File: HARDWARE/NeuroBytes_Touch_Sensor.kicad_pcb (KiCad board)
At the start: 2 copper layers, 52.3 x 34.9 mm, 25 parts, among them P12 CONN_01X07, P6 CONN_01X04, P7 CONN_01X04, Q1 NPN_dual, Q2 NPN_dual, SW1 SW_PUSH, SW2 SW_PUSH, U1 STM32L011Gx, U2 LD3985G33R

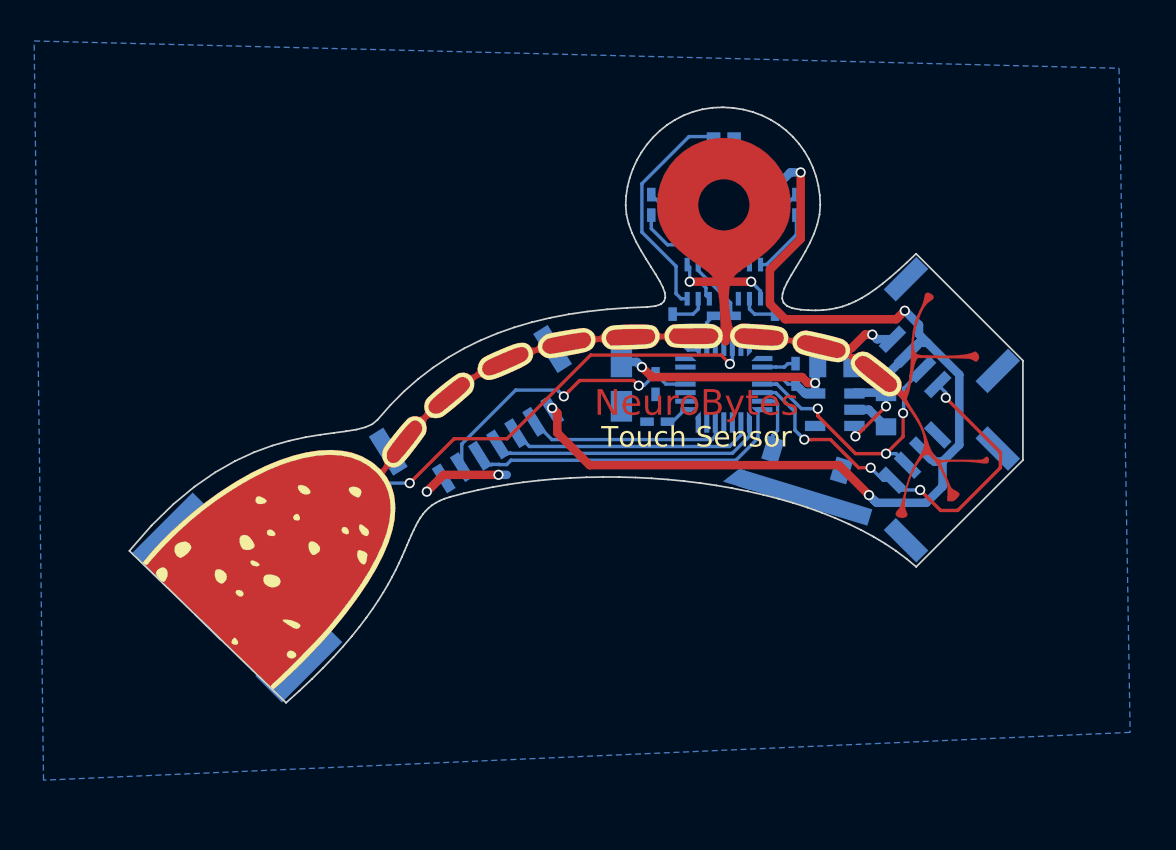
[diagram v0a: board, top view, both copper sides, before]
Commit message: Board rev2. Simplified PCB outline and modified axon graphics a bit.
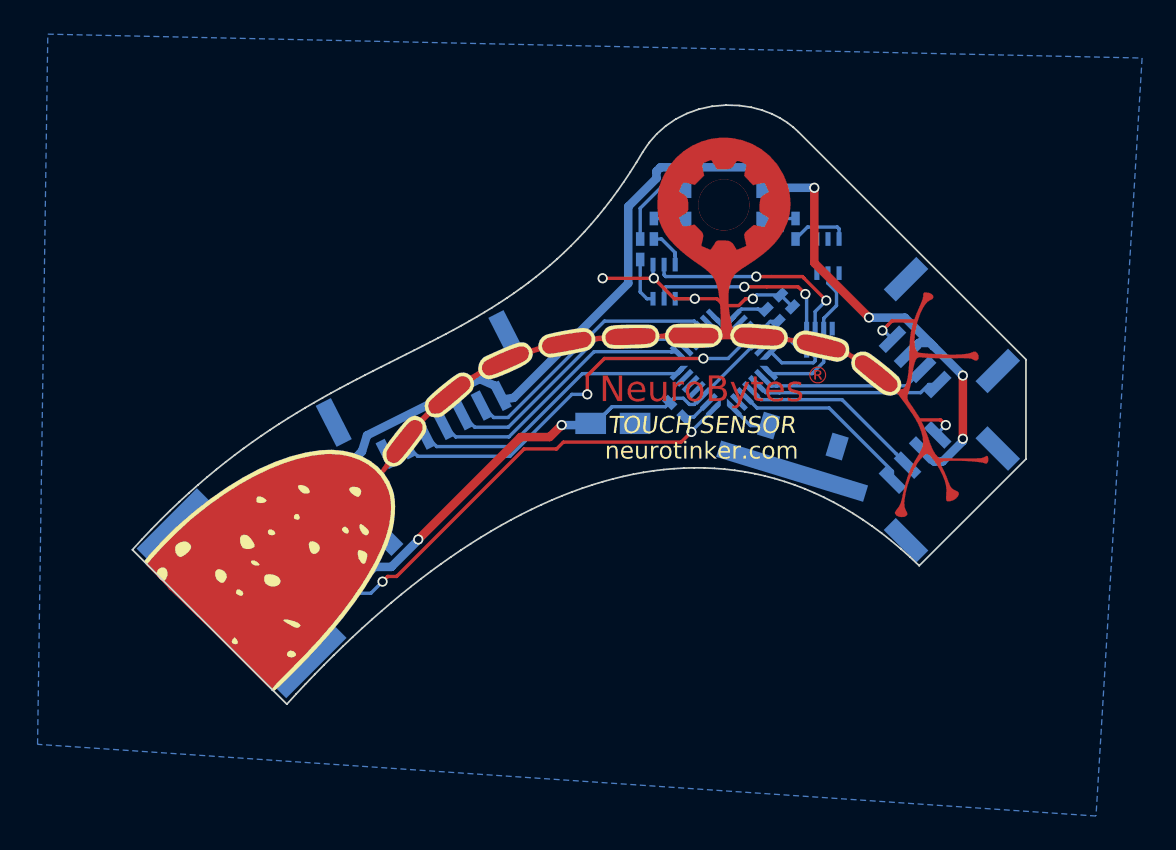
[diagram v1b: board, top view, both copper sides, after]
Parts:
- removed the G*** at (126.5, 69.5) (x3)
- removed R5, R6, R7: R, KiCad_Footprints:ZF_SMD_NonPol_0402
- added G***: LOGO, KiCad_Footprints:ZF_LOGO_Touch_Sensor, F.Cu at (126.5, 69.5)
- added RN1: R_Pack04, KiCad_Footprints:ZF_RN_4iso_CTS-0804, B.Cu at (132.1, 77.4)
- moved C1 33.6 mm to (102.8, 86.5), turned to 225 degrees
- moved U2 29.3 mm to (104.5, 88.2), turned to 315 degrees
- moved C4 28.9 mm to (106.2, 90.0), turned to 45 degrees
- moved R4 9.76 mm to (129.4, 75.2), turned to 225 degrees
- moved C5 8.64 mm to (130.1, 75.9), turned to 45 degrees
- moved R1 8.22 mm to (121.6, 72.1), turned to 270 degrees
- moved C3 7.26 mm to (123.8, 81.5), turned to 315 degrees
- moved Q2 4.84 mm to (132.6, 72.5)
- moved P12 3.25 mm to (109.0, 80.2), turned to 117 degrees
- moved C2 2.35 mm to (120.0, 82.3), turned to 0 degrees
- moved Q1 2.00 mm to (123.0, 74.0)
- moved SW1 1.42 mm to (130.4, 85.6)
- moved R2 1.41 mm to (122.4, 70.9)
- moved R3 1.40 mm to (130.7, 70.9)
- moved U1 1.25 mm to (126.5, 78.8), turned to 225 degrees
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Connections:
- P6 pad 3: AIN -> A1IN
- P6 pad 4: AEX -> A1EX
- P7 pad 3: AIN -> A2IN
- P7 pad 4: AEX -> A2EX
- U1 pad 10: Net-(U1-Pad10) -> A1EX
- U1 pad 11: LED_G -> A2IN
- U1 pad 12: INPUT -> A2EX
- U1 pad 14: Net-(U1-Pad14) -> IDENTIFY
- U1 pad 15: D1EX -> INPUT
- U1 pad 18: AIN -> Net-(U1-Pad18)
- U1 pad 19: AEX -> Net-(U1-Pad19)
- U1 pad 20: IDENTIFY -> Net-(U1-Pad20)
- U1 pad 6: Net-(U1-Pad6) -> LED_R
- U1 pad 7: Net-(U1-Pad7) -> LED_G
- U1 pad 9: LED_R -> A1IN
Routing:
- net AEX: track 24.9 -> 0.00 mm, vias 4 -> 0
- net AIN: track 16.7 -> 0.00 mm, vias 3 -> 0
- net +3V3: track 22.6 -> 34.8 mm
- net A1EX: track 0.00 -> 11.0 mm
- net A2IN: track 0.00 -> 11.0 mm
- net A2EX: track 0.00 -> 11.0 mm
- net Net-(Q1-Pad3): track 13.4 -> 2.82 mm
- net A1IN: track 0.00 -> 9.95 mm
- net RESET: track 17.0 -> 26.0 mm
- net Net-(Q1-Pad2): track 2.22 -> 11.1 mm, vias 0 -> 2
- net Net-(Q1-Pad5): track 3.87 -> 12.6 mm, vias 0 -> 2
- net INPUT: track 40.3 -> 32.2 mm
- net MOSI: track 11.9 -> 15.8 mm
- net Net-(Q1-Pad6): track 5.42 -> 2.38 mm
- net SWDIO/SCK: track 19.2 -> 16.8 mm
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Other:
- board size 52.3 x 34.9 mm -> 52.3 x 35.1 mm
- board text added: "ID"
- board text added: "TOUCH SENSOR"
- board text added: "®"
- board text removed: "Tactile Corpuscle"
- board text removed: "Touch Sensor"

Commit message: Updated PCB footprints to proper rotations. Added fab documentation to PCB file. Generated Gerber files, drill file, and placement file. Generated and filled in BOM. Added switch graphic to PCB dwgs layer.
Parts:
- added REF**: ZF_Fiducial-1mm, KiCad_Footprints:ZF_Fiducial-1mm, B.Cu at (98.2, 86.2)
- added REF**: ZF_Fiducial-1mm, KiCad_Footprints:ZF_Fiducial-1mm, B.Cu at (109.8, 86.2)
- moved SW1 0.14 mm to (130.5, 85.7)
- turned U1 to 315 degrees
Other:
- net class Default: clearance 0.2 -> 0.19
- rule trace_clearance: 0.2 -> 0.19
- board text added: "COMPONENT POSITION ORIGIN"
- board text added: "NOTES: 1. FOOTPRINTS ORIENTED PER IPC-7351FC LEVEL B (PIN 1 IN LOWER LEFT) 2. COMPONENT ORIENTATION IN DEGREES COUNTER-CLOCKWISE 3. COMPONENTS ARE MOUNTED ON B.CU LAYER ONLY 4. PCB IS 1.6mm FR4 RATED FOR ROHS REFLOW, 1OZ COPPER, ENIG FINISH 5. MATTE BLACK SOLDER MASK WITH WHITE SILKSCREEN 6. SOLDER PASTE MUST BE ROHS COMPLIANT (LEAD-FREE) 7. NO MARKS (E-TEST, QA, SERIAL NUMBER, ETC) ON FRONT (LOG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"
- board text added: "ROUTE BOARD OUTLINE EXCEPT FOR TWO ENDS"
- board text added: "SW2 (HORIZONTAL MTG)"
- board text added: "V-SCORE PARALLEL ENDS"
